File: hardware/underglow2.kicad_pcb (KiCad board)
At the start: 4 copper layers, 78.5 x 95 mm, 146 parts, among them J101 J_Delphi_Sicma_24, J501 Conn_ARM_SWD_TagConnect_TC203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, J502 Conn_ARM_SWD_TagConnect_TC2030, J601 Conn_ARM_SWD_TagConnect_TC203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, Q301 AO4803A, Q302 8205A, Q303 8205A, Q304 8205A, Q305 BC817, Q306 BC817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

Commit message: Add Case and other models
Signed-off-by: Connor Rigby <connorr@hey.com>
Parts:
- added Bottom: Bottom, Enclosure:Bottom, F.Cu at (25.0, 25.0)
- added SMA_Connector: SMA_Connector, Enclosure:SMA_Connector, F.Cu at (25.0, 25.0)
- added Top: Top, Enclosure:Top, F.Cu at (25.0, 25.0)
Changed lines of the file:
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@@
     )
   )
+  (footprint "Enclosure:Top" (layer "F.Cu")
+    (at 25 25)
+    (attr board_only exclude_from_pos_files exclude_from_bom)
+    (fp_text reference "Top" (at 0 -0.5 unlocked) (layer "F.SilkS") hide
+        (effects (font (size 1 1) (thickness 0.15)))
+    )
+    (fp_text value "Top" (at 0 -0.7 unlocked) (layer "F.Fab")
+        (effects (font (size 1 1) (thickness 0.15)))
+    )
+    (fp_text user "Top" (at 0 0.8 unlocked) (layer "F.Fab")
+        (effects (font (size 1 1) (thickness 0.15)))
+    )
+    (model "${KIPRJMOD}/library/Enclosure.pretty/packages3d/enclosure-top.step"
+      (opacity 0.8000)      (offset (xyz 39.5 -47.5 0))
+      (scale (xyz 1 1 1))
+      (rotate (xyz 0 0 0))
+    )
+  )
   (footprint "Resistor_SMD:R_0603_1608Metric" (layer "F.Cu")
     (at 80.555755 60.43 -90)
@@
     )
   )
+  (footprint "Enclosure:SMA_Connector" (layer "F.Cu")
+    (at 25 25)
+    (attr board_only exclude_from_pos_files exclude_from_bom)
+    (fp_text reference "SMA_Connector" (at 0 -0.5 unlocked) (layer "F.SilkS") hide
+        (effects (font (size 1 1) (thickness 0.15)))
+    )
+    (fp_text value "SMA_Connector" (at 15 -2.5 unlocked) (layer "F.Fab")
+        (effects (font (size 1 1) (thickness 0.15)))
+    )
+    (fp_text user "SMA_Connector" (at 15 -1 unlocked) (layer "F.Fab")
+        (effects (font (size 1 1) (thickness 0.15)))
+    )
+    (model "${KIPRJMOD}/library/LCSC_Antenna.pretty/packages3d/MH113-MH1RP-01SB1-0100.stp"
+      (offset (xyz 8 -19.5 8.5))
+      (scale (xyz 1 1 1))
+      (rotate (xyz 0 0 -90))
+    )
+    (model "${KIPRJMOD}/library/Enclosure.pretty/packages3d/enclosure-top.step"
+      (opacity 0.5300)      (offset (xyz 39.5 -47.5 0))
+      (scale (xyz 1 1 1))
+      (rotate (xyz 0 0 0))
+    )
+    (model "${KIPRJMOD}/library/LCSC_Antenna.pretty/packages3d/MH113-MH1RP-01SB1-0100.stp"
+      (offset (xyz 8 -19.5 19))
+      (scale (xyz 1 1 1))
+      (rotate (xyz 0 0 -90))
+    )
+    (model "${KIPRJMOD}/library/Enclosure.pretty/packages3d/Wifi_Antenna.step"
+      (offset (xyz 8 26.5 8.5))
+      (scale (xyz 1 1 1))
+      (rotate (xyz -180 0 0))
+    )
+    (model "${KIPRJMOD}/library/Enclosure.pretty/packages3d/Wifi_Antenna.step"
+      (offset (xyz 8 26 19))
+      (scale (xyz 1 1 1))
+      (rotate (xyz -180 0 0))
+    )
+  )
   (footprint "Package_TO_SOT_SMD:SOT-23-5" (layer "F.Cu")
     (at 60.47 50.48 90)
@@
     )
   )
+  (footprint "Enclosure:Bottom" (layer "F.Cu")
+    (at 25 25)
+    (attr board_only exclude_from_pos_files exclude_from_bom)
+    (fp_text reference "Bottom" (at 0 -0.5 unlocked) (layer "F.SilkS") hide
+        (effects (font (size 1 1) (thickness 0.15)))
+    )
+    (fp_text value "Bottom" (at 5 -0.6 unlocked) (layer "F.Fab")
+        (effects (font (size 1 1) (thickness 0.15)))
+    )
+    (fp_text user "Bottom" (at 5 0.9 unlocked) (layer "F.Fab")
+        (effects (font (size 1 1) (thickness 0.15)))
+    )
+    (model "${KIPRJMOD}/library/Enclosure.pretty/packages3d/enclosure-bottom.step"
+      (opacity 0.5000)      (offset (xyz 39.5 -47.5 0))
+      (scale (xyz 1 1 1))
+      (rotate (xyz 0 0 0))
+    )
+  )
   (footprint "Inductor_SMD:L_0402_1005Metric" (layer "F.Cu")
     (at 34 88 90)
@@
       (effects (font (size 1 1) (thickness 0.25) bold italic) (justify left top mirror))
   )
+  (dimension (type aligned) (layer "User.1")
+    (pts (xy 25 25) (xy 25 120))
+    (height 4.999999)
+    (gr_text "95.0000 mm" (at 18.850001 72.5 90) (layer "User.1")
+      (effects (font (size 1 1) (thickness 0.15)))
+    )
+    (format (prefix "") (suffix "") (units 3) (units_format 1) (precision 4))
+    (style (thickness 0.15) (arrow_length 1.27) (text_position_mode 0) (extension_height 0.58642) (extension_offset 0.5) keep_text_aligned)
+  )
+  (dimension (type aligned) (layer "User.1")
+    (pts (xy 25 20) (xy 104 20))
+    (height 0)
+    (gr_text "79.0000 mm" (at 64.5 18.85) (layer "User.1")
+      (effects (font (size 1 1) (thickness 0.15)))
+    )
+    (format (prefix "") (suffix "") (units 3) (units_format 1) (precision 4))
+    (style (thickness 0.15) (arrow_length 1.27) (text_position_mode 0) (extension_height 0.58642) (extension_offset 0.5) keep_text_aligned)
+  )
   (segment (start 46.03 54.3675) (end 46.03 56.26) (width 0.75) (layer "F.Cu") (net 1))

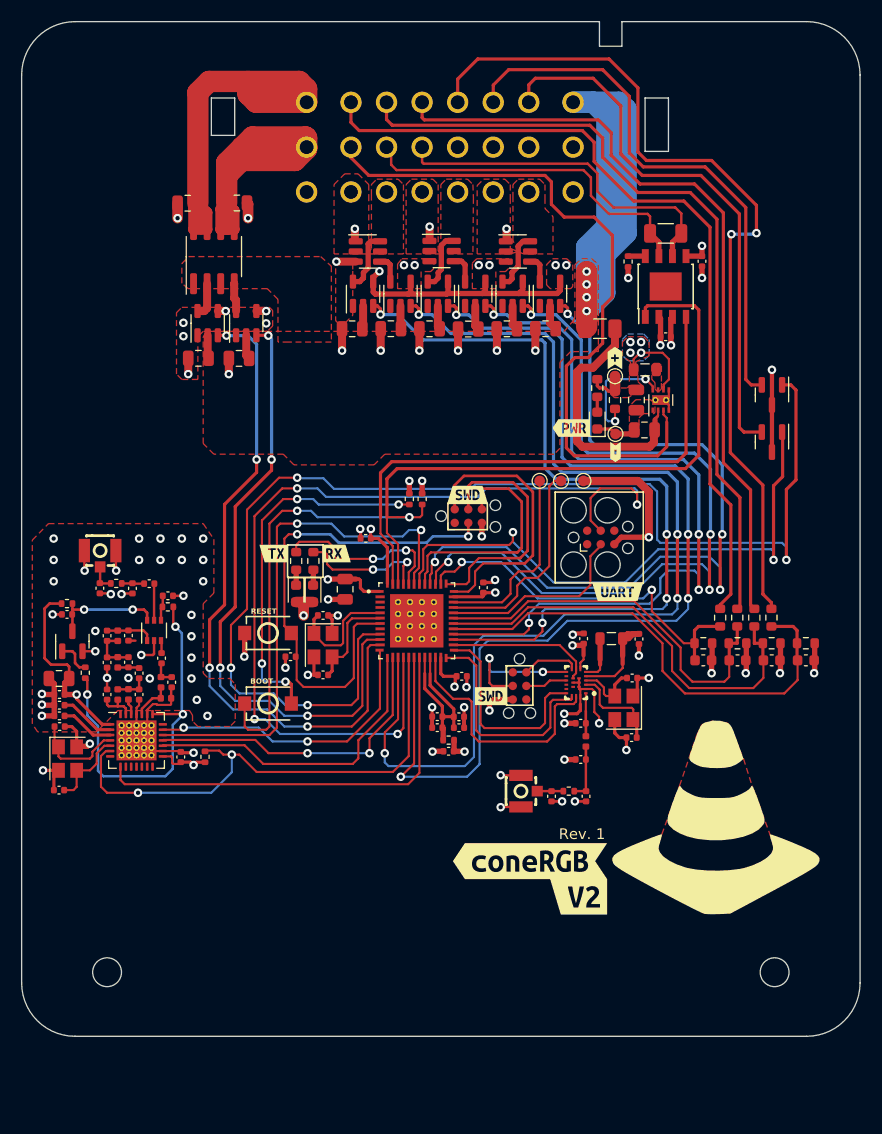
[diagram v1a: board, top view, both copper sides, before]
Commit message: More pre-production updates:
* fix USART connections being reversed
* add test points for SPI and BLE

Signed-off-by: Connor Rigby <connorr@hey.com>
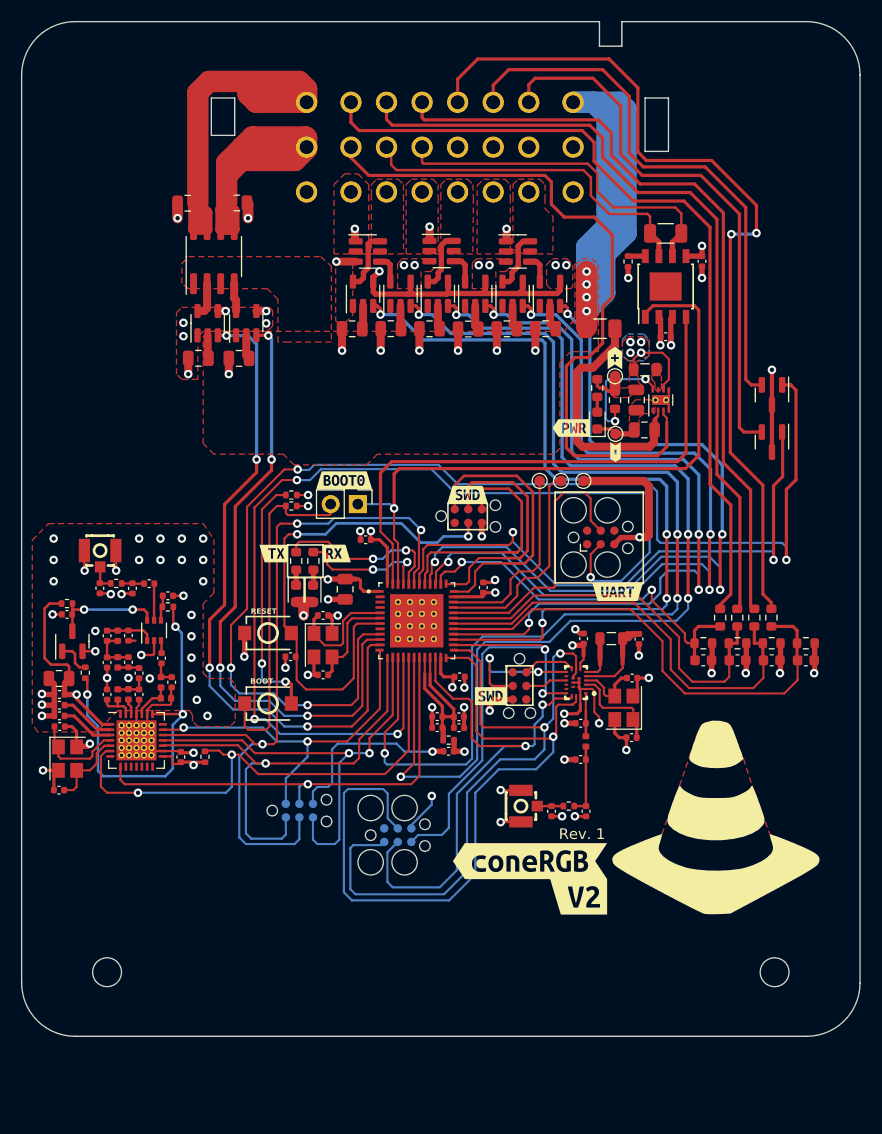
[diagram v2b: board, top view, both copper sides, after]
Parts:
- removed NT601: NetTie_2, NetTie:NetTie-2_SMD_Pad0.5mm
- added J503: BOOT0, Connector_PinHeader_2.54mm:PinHeader_1x02_P2.54mm_Vertical, F.Cu at (56.5, 70.2)
- added JBLE: Conn_ARM_SWD_TagConnect_TC2030, Connector:Tag-Connect_TC2030-IDC-FP_2x03_P1.27mm_Vertical, B.Cu at (60.2, 101.2)
- added JSPI: Conn_ARM_SWD_TagConnect_TC2030-NL, Connector:Tag-Connect_TC2030-IDC-NL_2x03_P1.27mm_Vertical, B.Cu at (51.0, 98.9)
- added kibuzzard-64154737: G***, kibuzzard-64154737, B.Cu at (58.2, 106.3)
- added kibuzzard-6419E4F0: G***, kibuzzard-6419E4F0, B.Cu at (51.0, 101.0)
- added kibuzzard-641A154C: G***, kibuzzard-641A154C, F.Cu at (55.2, 68.0)
- Bottom: value Bottom -> Case_Bottom
- SMA_Connector: value SMA_Connector -> SMA_Connector_Antenna
- Top: value Top -> Case_Top
- moved R502 12.3 mm to (50.2, 70.3), turned to 0 degrees
- moved R501 11.1 mm to (50.2, 69.3), turned to 0 degrees
- moved C605 1.40 mm to (77.8, 98.9)
- moved C606 1.40 mm to (74.6, 98.9)
- moved ANT601 1.40 mm to (71.8, 98.4)
- moved R601 1.40 mm to (76.2, 98.4)
- moved C50823 0.21 mm to (66.0, 86.3)
- moved C50848 0.12 mm to (57.2, 73.5)
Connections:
- J502 pad 3: /Application/USART1_RX -> /Application/USART1_TX
- J502 pad 4: /Application/USART1_TX -> /Application/USART1_RX
- U601 pad 15: /Application/LPUART1_RTS -> /Application/LPUART1_CTS
- U601 pad 16: /Application/LPUART1_TX -> /Application/LPUART1_RX
- U601 pad 17: /Application/LPUART1_RX -> /Application/LPUART1_TX
- U601 pad 22: /Application/LPUART1_CTS -> /Application/LPUART1_RTS
- U601 pad 8: /Application/LPUART1_CTS -> /Application/LPUART1_RTS
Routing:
- net /Application/LPUART1_TX: track 21.3 -> 71.2 mm, vias 0 -> 1
- net /Application/LPUART1_RTS: track 19.7 -> 64.0 mm, vias 0 -> 2
- net /Application/LPUART1_CTS: track 13.8 -> 43.1 mm, vias 0 -> 2
- net /Application/LPUART1_RX: track 23.0 -> 50.1 mm, vias 0 -> 2
- net GND: track 179.1 -> 199.0 mm, vias 96 -> 97
- net /Application/SPI1_MOSI: track 49.5 -> 69.2 mm, vias 2 -> 3
- net /Application/SPI1_SCK: track 29.8 -> 43.6 mm, vias 0 -> 1
- net /Application/SPI1_MISO: track 29.7 -> 43.0 mm
- net Net-(BTN502-Pad2): track 34.4 -> 23.4 mm, vias 4 -> 2
- net /Application/BOOT0: track 40.9 -> 32.4 mm, vias 2 -> 0
- net /Application/USART1_RX: track 18.0 -> 25.9 mm
- net /Application/USART1_TX: track 88.7 -> 96.4 mm
- net +3.3V: track 269.6 -> 276.7 mm
- net /Application/SPI1_NSS: track 27.4 -> 34.1 mm
- net /Application/SPI1_IRQ: track 40.6 -> 43.3 mm, vias 0 -> 1
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- removed copper zone on In2.Cu, net GND

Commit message: Submitted for production
Signed-off-by: Connor Rigby <connorr@hey.com>
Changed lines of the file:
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@@
     (attr board_only exclude_from_pos_files exclude_from_bom)
     (fp_text reference "kibuzzard-641A154C" (at 0 -3.891492) (layer "F.SilkS") hide
-        (effects (font (size 0 0)))
+        (effects (font (size 0 0) (thickness 0.15)))
     )
     (fp_text value "G***" (at 0 3.891492) (layer "F.SilkS") hide
-        (effects (font (size 0 0)))
+        (effects (font (size 0 0) (thickness 0.15)))
     )
     (fp_poly
@@
     (pad "49" thru_hole circle (at 1.6 1.7) (size 0.6 0.6) (drill 0.3) (layers "*.Cu" "*.Mask")
       (net 2 "GND") (pinfunction "EP") (pintype "power_in"))
-    (model "${KIPRJMOD}/library/LCSC_Microcontroller.pretty/packages3d/QFN50P700X700X60-49N.step" hide
+    (model "${KIPRJMOD}/library/LCSC_Microcontroller.pretty/packages3d/QFN50P700X700X60-49N.step"
       (offset (xyz 0 0 0))
       (scale (xyz 1 1 1))
       (rotate (xyz -90 0 0))
     )
-    (model "${KIPRJMOD}/library/LCSC_Microcontroller.pretty/packages3d/UFQFPN-48_L7.0-W7.0-P0.50-BL-EP.wrl"
+    (model "${KIPRJMOD}/library/LCSC_Microcontroller.pretty/packages3d/UFQFPN-48_L7.0-W7.0-P0.50-BL-EP.wrl" hide
       (offset (xyz 0 0 0))
       (scale (xyz 1 1 1))
@@
     (attr board_only exclude_from_pos_files exclude_from_bom)
     (fp_text reference "kibuzzard-6419E4F0" (at 0 3.891492) (layer "B.SilkS") hide
-        (effects (font (size 0 0)) (justify mirror))
+        (effects (font (size 0 0) (thickness 0.15)) (justify mirror))
     )
     (fp_text value "G***" (at 0 -3.891492) (layer "B.SilkS") hide
-        (effects (font (size 0 0)) (justify mirror))
+        (effects (font (size 0 0) (thickness 0.15)) (justify mirror))
     )
     (fp_poly
@@
       (stroke (width 0) (type solid)) (fill solid) (layer "B.SilkS"))
   )
-  (gr_rect (start 55.85 105.425) (end 64.1 96.925)
+  (gr_rect (start 55.85 96.925) (end 64.1 105.425)
     (stroke (width 0.15) (type default)) (fill none) (layer "B.SilkS"))
   (gr_poly
@@
   (segment (start 71.93 45.57) (end 72.6075 45.57) (width 0.5) (layer "F.Cu") (net 74))
   (segment (start 83.395 46.955) (end 81.78 46.955) (width 0.5) (layer "F.Cu") (net 75))
+  (segment (start 83.395 52.645) (end 83.395 51.83) (width 0.3) (layer "F.Cu") (net 76))
   (segment (start 88.4 52) (end 88.4 65.6) (width 0.3) (layer "F.Cu") (net 76))
-  (segment (start 59.875 70.575) (end 59.875 70.574998) (width 0.2) (layer "F.Cu") (net 76))
   (segment (start 87.15 66.85) (end 60.375 66.85) (width 0.3) (layer "F.Cu") (net 76))
-  (segment (start 60.244707 77.669073) (end 60.244707 73.819707) (width 0.2) (layer "F.Cu") (net 76))
   (segment (start 59.875 67.35) (end 59.875 70.574998) (width 0.3) (layer "F.Cu") (net 76))
-  (segment (start 88.4 65.6) (end 87.15 66.85) (width 0.3) (layer "F.Cu") (net 76))
-  (segment (start 84.11 51.6) (end 88 51.6) (width 0.3) (layer "F.Cu") (net 76))
+  (segment (start 83.625 51.6) (end 88 51.6) (width 0.3) (layer "F.Cu") (net 76))
+  (segment (start 59.875 70.575) (end 59.875 70.574998) (width 0.2) (layer "F.Cu") (net 76))
+  (segment (start 60.244707 77.669073) (end 60.244707 73.819707) (width 0.2) (layer "F.Cu") (net 76))
   (segment (start 59.875 73.45) (end 59.875 70.575) (width 0.2) (layer "F.Cu") (net 76))
+  (segment (start 83.395 51.83) (end 83.625 51.6) (width 0.3) (layer "F.Cu") (net 76))
   (segment (start 60.244707 73.819707) (end 59.875 73.45) (width 0.2) (layer "F.Cu") (net 76))
-  (segment (start 83.395 52.645) (end 83.395 52.315) (width 0.3) (layer "F.Cu") (net 76))
-  (segment (start 88 51.6) (end 88.4 52) (width 0.3) (layer "F.Cu") (net 76))
+  (segment (start 88.4 65.6) (end 87.15 66.85) (width 0.3) (layer "F.Cu") (net 76))
   (segment (start 60.375 66.85) (end 59.875 67.35) (width 0.3) (layer "F.Cu") (net 76))
-  (segment (start 83.395 52.315) (end 84.11 51.6) (width 0.3) (layer "F.Cu") (net 76))
+  (segment (start 88 51.6) (end 88.4 52) (width 0.3) (layer "F.Cu") (net 76))
   (via (at 59.875 70.575) (size 0.8) (drill 0.4) (layers "F.Cu" "B.Cu") (net 76))
   (segment (start 59.475 70.175) (end 59.875 70.575) (width 0.2) (layer "B.Cu") (net 76))

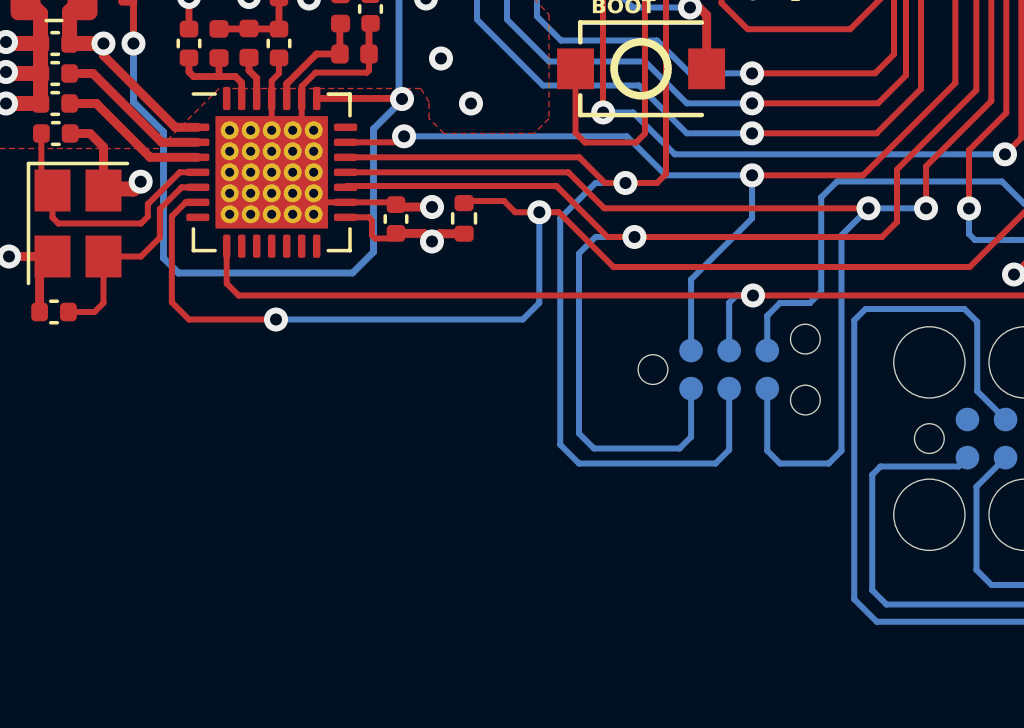
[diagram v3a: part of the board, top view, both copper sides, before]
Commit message: hardware: Add flash storage
Signed-off-by: Connor Rigby <connorr@hey.com>
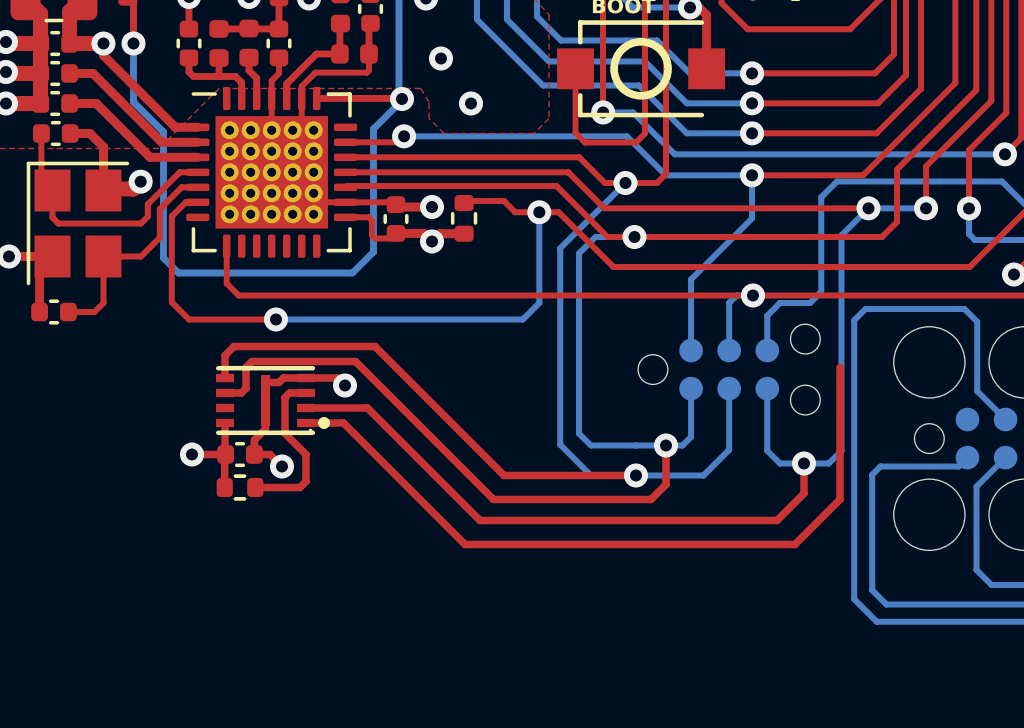
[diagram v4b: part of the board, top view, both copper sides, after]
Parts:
- added C501: C_0402_100nf_X7R, Capacitor_SMD:C_0402_1005Metric, F.Cu at (34.7, 101.7)
- added R505: R_0402_1k, Resistor_SMD:R_0402_1005Metric, F.Cu at (34.7, 102.8)
- added U502: W25X10CLUXIG, LCSC_Microcontroller:USON-8_L3.0-W2.0-P0.50-BL-EP-1, F.Cu at (35.6, 99.9)
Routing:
- net unconnected-(U502-CS#-Pad1): track 0.00 -> 24.5 mm
- net /Application/SPI1_MISO: track 43.0 -> 62.6 mm, vias 2 -> 3
- net /Application/SPI1_SCK: track 43.6 -> 62.5 mm, vias 1 -> 2
- net /Application/SPI1_MOSI: track 69.2 -> 85.3 mm, vias 3 -> 4
- net GND: track 199.0 -> 204.7 mm, vias 97 -> 99
- net Net-(U502-WP#): track 0.00 -> 5.63 mm
- net +3.3V: track 276.7 -> 280.0 mm, vias 17 -> 18
